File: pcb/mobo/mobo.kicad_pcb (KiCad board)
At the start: 2 copper layers, 51.6 x 89 mm, 72 parts, among them J1 SWD_10, J2 PEEL_MOTOR, J3 DRIVE_MOTOR, J4 SW1, J5 SPRING_FINGERS, J6 SW2, J7 SW1, J8 USART1, J9 SWD_10, U1 STM32F031C6Tx, U2 STM32F031K6Ux, U4 AP1117-33, U5 MC34063AD, U6 MAX3078E, U7 DRV8837, U8 DRV8837, Y1 8MHz

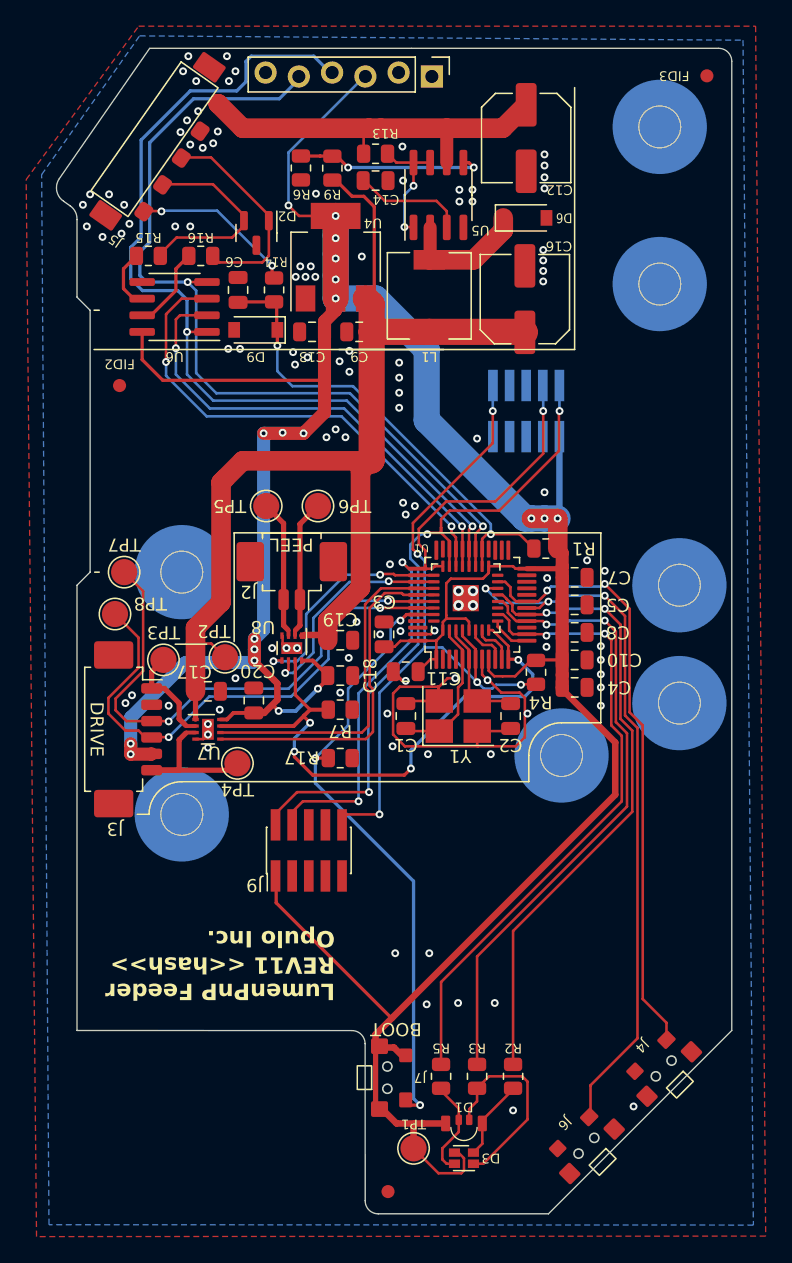
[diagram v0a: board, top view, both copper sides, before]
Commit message: Cost optimize main feeder pcb
- Change mcu/logic supply to 5V instead of 3.3V
- Use atmega328p as mcu
- Use SP308xE as RS485 transceiver
- Use 100uF output capacitor for buck coverter
- Make it possible to use solderable standoffs instead of chamfers
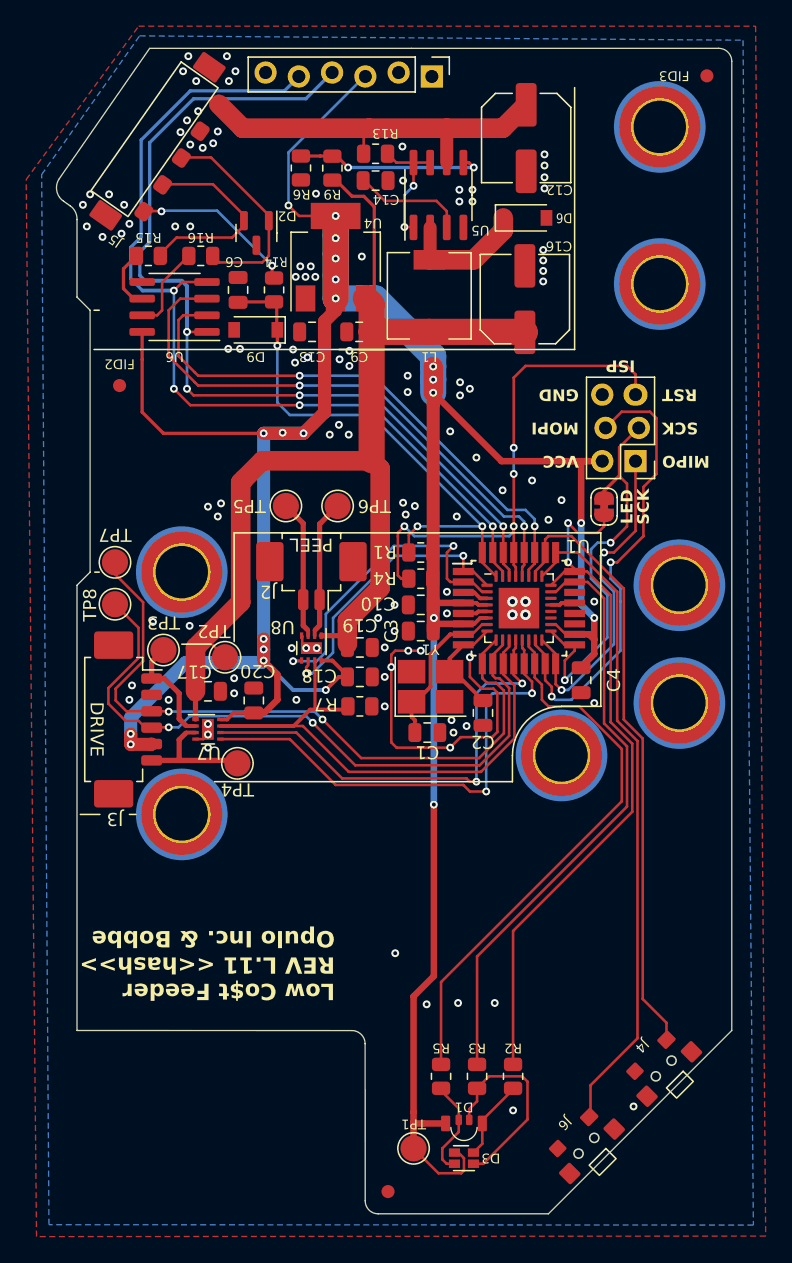
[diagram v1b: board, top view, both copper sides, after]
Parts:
- removed C11, C8: 4.7uF, Capacitor_SMD:C_0805_2012Metric
- removed C5, C7: 100n, Capacitor_SMD:C_0805_2012Metric
- removed the G*** at (107.0, 61.5)
- removed the G*** at (107.7, 98.4)
- removed J7: SW1, feeder:1TS003B-1400-3500A-CT
- removed J9: SWD_10, feeder:SWD-No-Paste
- removed R17: 10K, Resistor_SMD:R_0805_2012Metric
- removed REF**: OSHW-Symbol_6.7x6mm_Mask, feeder:OSHW-Symbol_6.7x6mm_Mask
- added H1: Hole1, feeder:MountingHole_4.2mm_24822, F.Cu at (145.8, 35.8)
- added H2: Hole2, feeder:MountingHole_4.2mm_24822, F.Cu at (145.8, 47.8)
- added H3: Hole3, feeder:MountingHole_4.2mm_24822, F.Cu at (109.3, 69.8)
- added H4: Hole4, feeder:MountingHole_4.2mm_24822, F.Cu at (147.3, 70.8)
- added H5: Hole5, feeder:MountingHole_4.2mm_24822, F.Cu at (109.3, 88.3)
- added H6: Hole6, feeder:MountingHole_4.2mm_24822, F.Cu at (138.3, 83.8)
- added H7: Hole7, feeder:MountingHole_4.2mm_24822, F.Cu at (147.3, 79.8)
- added JP1: SCK_INDICATOR, Jumper:SolderJumper-2_P1.3mm_Bridged_RoundedPad1.0x1.5mm, F.Cu at (141.6, 64.8)
- C1, C2: value 15p -> 22p
- C10: value 4.7uF -> 10uF
- C16: value 470uF -> 100uF
- D9: value MMSZ4684T1G -> MMSZ4689T1G
- J1: value SWD_10 -> ISP; footprint Connector_PinHeader_1.27mm:PinHeader_2x05_P1.27mm_Vertical_SMD -> feeder:ISP_FRICTION_FIT; moved to F.Cu
- R2, R3, R5: value 470 -> 1k
- TP1: value TP_3V3 -> TP_5V
- U1: value STM32F031C6Tx -> ATmega328P-A; footprint Package_QFP:LQFP-48_7x7mm_P0.5mm -> Package_QFP:TQFP-32_7x7mm_P0.8mm
- U2: value STM32F031K6Ux -> ATmega328P-M; footprint feeder:QFN-32-No-Paste -> Package_DFN_QFN:QFN-32-1EP_5x5mm_P0.5mm_EP3.1x3.1mm
- U4: value AP1117-33 -> AP1117-50
- U6: value MAX3078E -> SP308xE
- Y1: value 8MHz -> 16MHz
- moved C10 12.5 mm to (127.5, 72.3), turned to 0 degrees
- moved R4 11.3 mm to (127.5, 70.3), turned to 0 degrees
- moved R1 9.55 mm to (127.5, 68.3)
- moved J1 9.30 mm to (144.1, 61.3), turned to 180 degrees
- moved U2 4.13 mm to (135.1, 72.5), turned to 0 degrees
- moved U1 3.57 mm to (135.1, 72.5), turned to 0 degrees
- moved Y1 3.08 mm to (128.3, 78.5)
- moved C3 2.81 mm to (127.5, 74.3), turned to 0 degrees
- moved C2 2.13 mm to (132.3, 80.5)
- moved C1 2.07 mm to (128.1, 82.0), turned to 0 degrees
- moved C19 1.60 mm to (122.9, 75.5)
- moved R7 1.52 mm to (122.9, 80.0)
- moved C18 1.50 mm to (122.9, 77.8)
- moved J2 1.50 mm to (119.2, 69.5)
- moved TP5 1.50 mm to (117.2, 64.8)
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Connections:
- C10 pad 2: +3V3 -> +5V
- C13 pad 1: +3V3 -> +5V
- C18 pad 2: +3V3 -> +5V
- C20 pad 2: +3V3 -> +5V
- C3 pad 2: +3V3 -> +5V
- C4 pad 2: +3V3 -> +5V
- D1 pad 1: +3V3 -> +5V
- D3 pad 4: +3V3 -> +5V
- J1 pad 1: +3V3 -> MIPO
- J1 pad 2: SWDIO -> +5V
- J1 pad 3: GND -> SCK
- J1 pad 4: SWCLK -> MOPI
- J1 pad 5: GND -> RESET
- J1 pad 6: unconnected-(J1-Pad6) -> GND
- J3 pad 5: +3V3 -> +5V
- J8 pad 3: +3V3 -> +5V
- R1 pad 2: +3V3 -> +5V
- R4 pad 2: +3V3 -> +5V
- TP1 pad 1: +3V3 -> +5V
- U1 pad 1: +3V3 -> PEEL1
- U1 pad 10: PA0 -> DRIVE_QUAD_B
- U1 pad 11: PA1 -> MOTOR_ENABLE
- U1 pad 12: MOTOR_ENABLE -> DRIVE1
- U1 pad 13: PA3 -> DRIVE2
- U1 pad 15: unconnected-(U1-Pad15) -> MOPI
- U1 pad 16: LED_G -> MIPO
- U1 pad 17: LED_R -> SCK
- U1 pad 18: SW2 -> +5V
- U1 pad 19: SW1 -> unconnected-(U1-ADC6-Pad19)
- U1 pad 2: unconnected-(U1-Pad2) -> PEEL2
- U1 pad 21: unconnected-(U1-Pad21) -> GND
- U1 pad 23: GND -> LED_G
- U1 pad 24: +3V3 -> LED_R
- U1 pad 25: unconnected-(U1-Pad25) -> SW2
- U1 pad 26: unconnected-(U1-Pad26) -> SW1
- U1 pad 27: unconnected-(U1-Pad27) -> ~{RE}
- U1 pad 28: unconnected-(U1-Pad28) -> DE
- U1 pad 29: 1WIRE -> RESET
- U1 pad 3: unconnected-(U1-Pad3) -> GND
- U1 pad 30: MCU_TX -> MCU_RX
- U1 pad 31: MCU_RX -> MCU_TX
- U1 pad 32: ~{RE} -> 1WIRE
- U1 pad 4: unconnected-(U1-Pad4) -> +5V
- U1 pad 5: OSC_IN -> GND
- U1 pad 6: OSC_OUT -> +5V
- U1 pad 7: RESET -> OSC_IN
- U1 pad 8: GND -> OSC_OUT
- U1 pad 9: +3V3 -> DRIVE_QUAD_A
- U2 pad 1: +3V3 -> PEEL1
- U2 pad 10: LED_B -> DRIVE_QUAD_B
- U2 pad 11: unconnected-(U2-Pad11) -> MOTOR_ENABLE
- U2 pad 12: LED_G -> DRIVE1
- U2 pad 13: LED_R -> DRIVE2
- U2 pad 14: SW2 -> LED_B
- U2 pad 15: SW1 -> MOPI
- U2 pad 16: unconnected-(U2-Pad16) -> MIPO
- U2 pad 17: +3V3 -> SCK
- U2 pad 18: 1WIRE -> +5V
- U2 pad 19: MCU_TX -> unconnected-(U2-ADC6-Pad19)
- U2 pad 2: OSC_IN -> PEEL2
- U2 pad 20: MCU_RX -> unconnected-(U2-AREF-Pad20)
- U2 pad 21: ~{RE} -> GND
- U2 pad 22: DE -> unconnected-(U2-ADC7-Pad22)
- U2 pad 23: SWDIO -> LED_G
- U2 pad 24: SWCLK -> LED_R
- U2 pad 25: PEEL2 -> SW2
- U2 pad 26: PEEL1 -> SW1
- U2 pad 27: DRIVE1 -> ~{RE}
- U2 pad 28: DRIVE2 -> DE
- U2 pad 29: DRIVE_QUAD_A -> RESET
- U2 pad 3: OSC_OUT -> GND
- U2 pad 30: DRIVE_QUAD_B -> MCU_RX
- U2 pad 31: BOOT0 -> MCU_TX
- U2 pad 32: unconnected-(U2-Pad32) -> 1WIRE
- U2 pad 4: RESET -> +5V
- U2 pad 5: +3V3 -> GND
- U2 pad 6: PA0 -> +5V
- U2 pad 7: PA1 -> OSC_IN
- U2 pad 8: MOTOR_ENABLE -> OSC_OUT
- U2 pad 9: PA3 -> DRIVE_QUAD_A
- U4 pad 2: +3V3 -> +5V
- U6 pad 8: +3V3 -> +5V
- U7 pad 8: +3V3 -> +5V
- U8 pad 8: +3V3 -> +5V
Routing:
- net +3V3: track 269.4 -> 0.00 mm, vias 19 -> 0
- net +5V: track 0.00 -> 244.5 mm, vias 0 -> 22
- net SWDIO: track 52.5 -> 0.00 mm, vias 3 -> 0
- net SWCLK: track 50.8 -> 0.00 mm, vias 3 -> 0
- net BOOT0: track 48.1 -> 0.00 mm, vias 3 -> 0
- net MOPI: track 0.00 -> 36.1 mm, vias 0 -> 2
- net SCK: track 0.00 -> 31.2 mm, vias 0 -> 2
- net MIPO: track 0.00 -> 25.8 mm, vias 0 -> 2
- net RESET: track 54.9 -> 40.8 mm, vias 5 -> 4
- net DRIVE_QUAD_B: track 40.4 -> 51.8 mm
- net DRIVE_QUAD_A: track 41.9 -> 53.2 mm
- net DRIVE2: track 26.8 -> 37.0 mm, vias 0 -> 2
- net DRIVE1: track 26.6 -> 35.3 mm, vias 0 -> 2
- net PEEL2: track 17.3 -> 24.4 mm
- net GND: track 39.6 -> 32.9 mm, vias 110 -> 115
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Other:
- outline, holes or cut-outs redrawn
- board text added: "GND"
- board text added: "ISP"
- board text added: "LED"
- board text added: "Low Co$t Feeder REV L.11 <<hash>> Opulo Inc. & Bobbe"
- board text added: "MIPO"
- board text added: "MOPI"
- board text added: "RST"
- board text added: "SCK"
- board text added: "U1"
- board text added: "VCC"
- board text removed: "BOOT"
- board text removed: "LumenPnP Feeder REV11 <<hash>> Opulo Inc."
